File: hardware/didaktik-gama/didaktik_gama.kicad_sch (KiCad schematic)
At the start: 165 parts, among them J1 Klávesnice, J2 MG, J4 Porty 8255, J5 Napájení 9–12V DC, J7 VGA DE-15 (RGB 15 kHz), J8 RGB z modulu ULA, SW1 RESET, T1 KSY72, T2 KSY72, T3 KC507, U1 UA880D (Z80), U10 4164, U11 4164, U12 4164, U13 4164, U14 4164, U15 4164, U16 4164, U17 2118, U18 2118, U19 2118, U2 27128 (16K EPROM), U20 2118, U21 2118, U22 2118, U23 2118, U24 2118, U25 74LS04, U26 74LS04, U27 74LS00, U28 74LS10, U29 74LS32, U3 8255 (MHB8255), U32 R-78E5.0-1.0 (spínaný, náhrad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, U37 74HCT244, U38 74HCT08, U4 ULA, U5 74LS157, U6 74LS157, U7 74LS157, U8 74LS157, U9 4164, Y1 14MHz

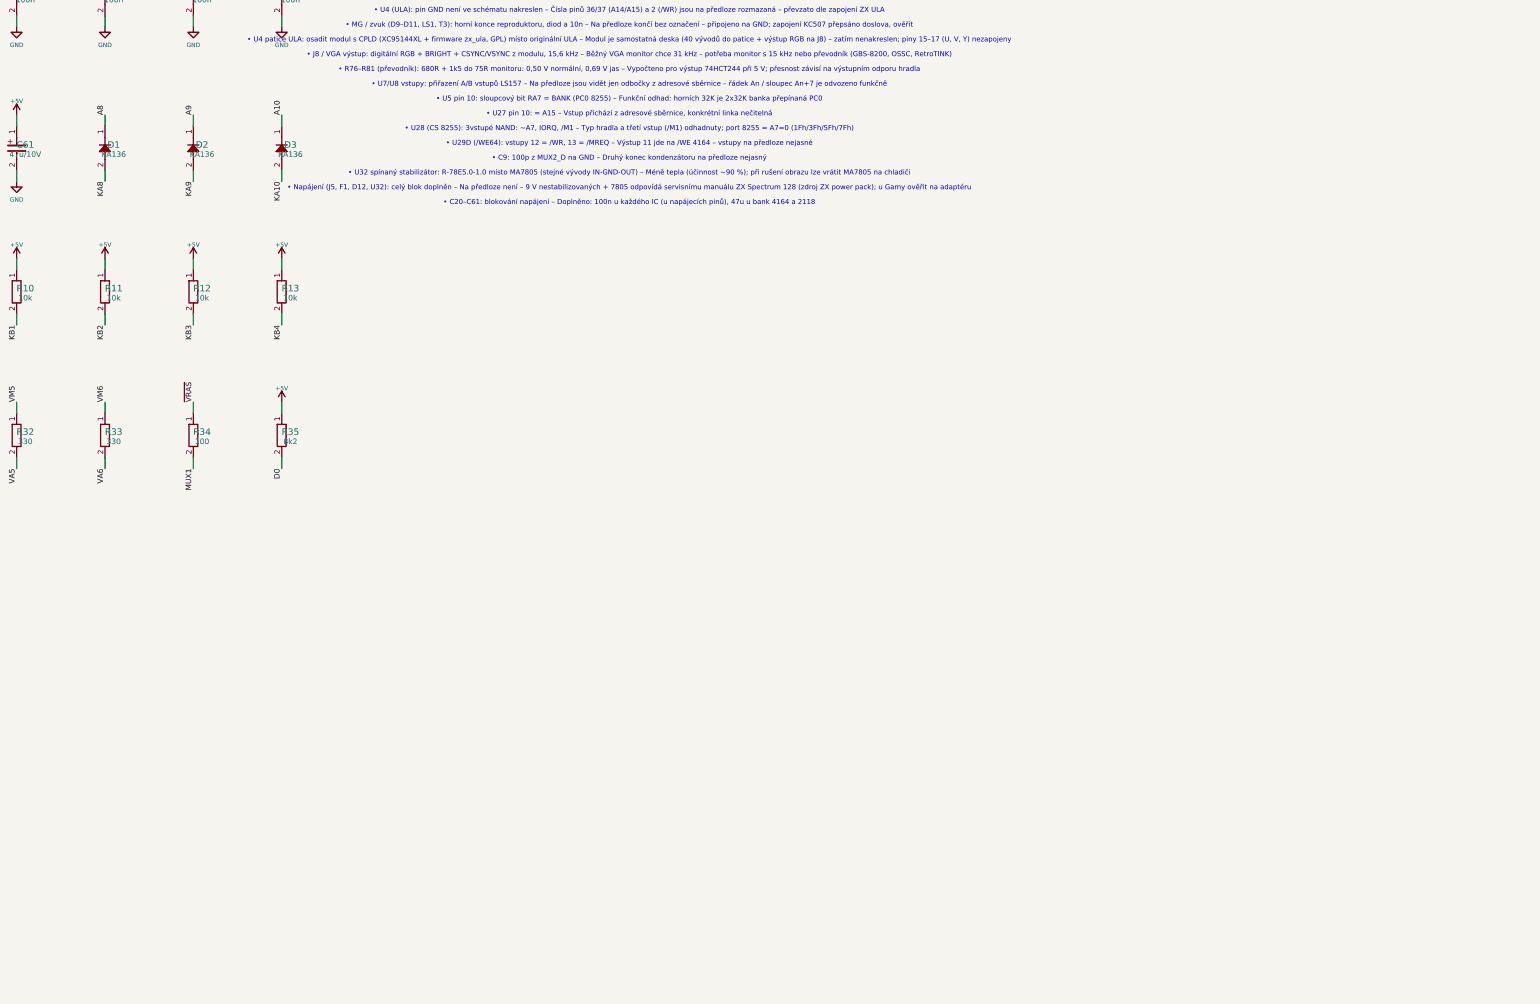
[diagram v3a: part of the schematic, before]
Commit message: Add USB keyboard interface (RPi Pico as USB host emulating the matrix)
Pico reads A8-A15 through 74LVC245 and pulls KB1-KB5 low through
open-drain 74LVC07, in parallel with the original keyboard; spare
buffer drives /RESET.

Co-Authored-By: Claude Opus 5.5 <noreply@anthropic.com>
Claude-Session: https://claude.ai/code/session_01LAVM7Gq9EYiUXiCEdy9ZRx
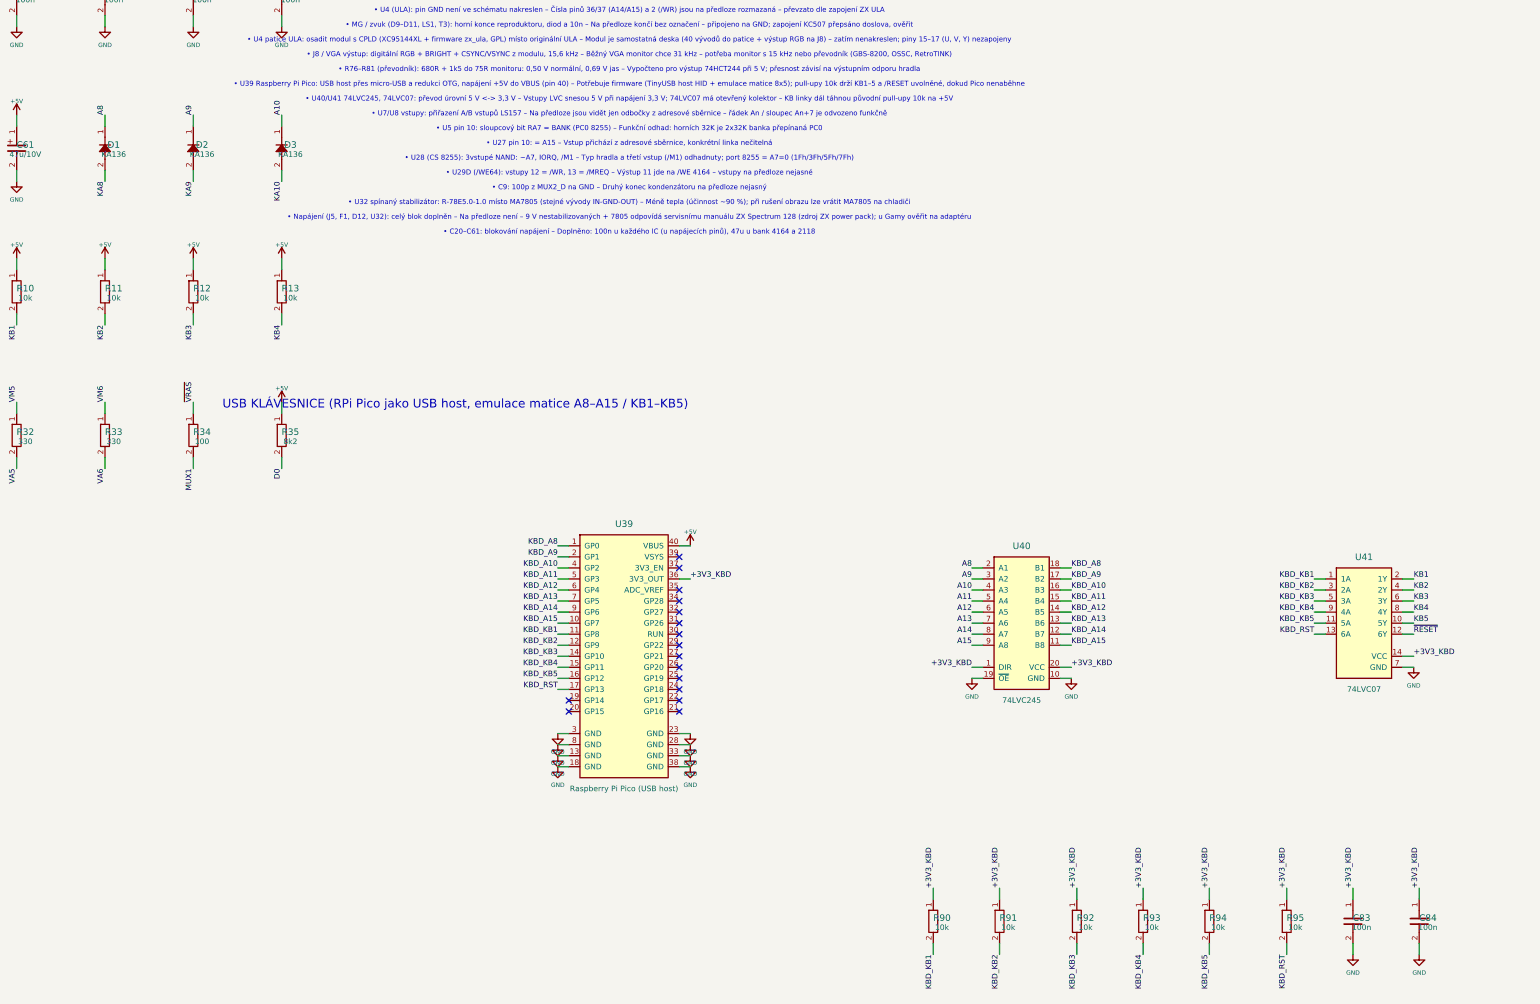
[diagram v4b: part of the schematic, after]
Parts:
- removed C12: 100n, Capacitor_THT:C_Disc_D5.0mm_W2.5mm_P5.00mm, symbol gama:C
- removed R19: 470, Resistor_THT:R_Axial_DIN0207_L6.3mm_D2.5mm_P10.16mm_Horizontal, symbol gama:R
- removed R33: 330, Resistor_THT:R_Axial_DIN0207_L6.3mm_D2.5mm_P10.16mm_Horizontal, symbol gama:R
- removed unit 2 of U25
- removed unit 4 of U28
- removed U32: R-78E5.0-1.0 (spínaný, náhrada 7805), Converter_DCDC:Converter_DCDC_RECOM_R-78E-0.5_THT, symbol gama:7805
- added C21, C44, C45, C83, C84: 100n, Capacitor_THT:C_Disc_D5.0mm_W2.5mm_P5.00mm, symbol gama:C
- added J5: Napájení 9–12V DC, Connector_BarrelJack:BarrelJack_Horizontal, symbol gama:CONN_2
- added R41: 8k2, Resistor_THT:R_Axial_DIN0207_L6.3mm_D2.5mm_P10.16mm_Horizontal, symbol gama:R
- added R90, R91, R92, R93, R94, R95: 10k, Resistor_THT:R_Axial_DIN0207_L6.3mm_D2.5mm_P10.16mm_Horizontal, symbol gama:R
- added U39: Raspberry Pi Pico (USB host), symbol gama:PICO
- added U40: 74LVC245, Package_SO:SOIC-20W_7.5x12.8mm_P1.27mm, symbol gama:74LVC245
- added U41: 74LVC07, Package_SO:SOIC-14_3.9x8.7mm_P1.27mm, symbol gama:74LVC07
- added U6: 74LS157, Package_DIP:DIP-16_W7.62mm, symbol gama:74LS157
- R19: renamed from U6; value 74LS157 -> 470; footprint Package_DIP:DIP-16_W7.62mm -> Resistor_THT:R_Axial_DIN0207_L6.3mm_D2.5mm_P10.16mm_Horizontal; symbol gama:74LS157 -> gama:R
- R33: renamed from U12; value 4164 -> 330; footprint Package_DIP:DIP-16_W7.62mm -> Resistor_THT:R_Axial_DIN0207_L6.3mm_D2.5mm_P10.16mm_Horizontal; symbol gama:4164 -> gama:R
- U12: renamed from R41; value 8k2 -> 4164; footprint Resistor_THT:R_Axial_DIN0207_L6.3mm_D2.5mm_P10.16mm_Horizontal -> Package_DIP:DIP-16_W7.62mm; symbol gama:R -> gama:4164
- U25: renamed from J5; value Napájení 9–12V DC -> 74LS04; footprint Connector_BarrelJack:BarrelJack_Horizontal -> Package_DIP:DIP-14_W7.62mm; symbol gama:CONN_2 -> gama:7404
- U28: renamed from C21; value 100n -> 74LS10; footprint Capacitor_THT:C_Disc_D5.0mm_W2.5mm_P5.00mm -> Package_DIP:DIP-14_W7.62mm; symbol gama:C -> gama:7410
- U32: renamed from C45; value 100n -> R-78E5.0-1.0 (spínaný, náhrada 7805); footprint Capacitor_THT:C_Disc_D5.0mm_W2.5mm_P5.00mm -> Converter_DCDC:Converter_DCDC_RECOM_R-78E-0.5_THT; symbol gama:C -> gama:7805
- renumbered C44 to C12
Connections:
- net +5V: now also U12.8 (VCC), U28.14 (VCC), U32.3 (OUT), C21.1, C44.1, C45.1, R41.1, U39.40 (VBUS), U6.16 (VCC); no longer C12.1, R19.16 (VCC), R33.8 (VCC), U12.1, U28.1, U32.1
- net A10: now also U40.4 (A3)
- net A11: now also U40.5 (A4), U6.10 (3B); no longer R19.10 (3B)
- net A12: now also U40.6 (A5), U6.6 (2B); no longer R19.6 (2B)
- net A13: now also U40.7 (A6), U6.3 (1B); no longer R19.3 (1B)
- net A14: now also U40.8 (A7), U6.13 (4B); no longer R19.13 (4B)
- net A15: now also U40.9 (A8)
- net A3: now also U6.11 (3A); no longer R19.11 (3A)
- net A4: now also U6.5 (2A); no longer R19.5 (2A)
- net A5: now also U6.2 (1A); no longer R19.2 (1A)
- net A6: now also U6.14 (4A); no longer R19.14 (4A)
- net A8: now also U40.2 (A1)
- net A9: now also U40.3 (A2)
- net D0: now also R19.1
- net D3: now also U12.14 (Q), U12.2 (D); no longer R33.14 (Q), R33.2 (D)
- net D6: now also R41.2; no longer U12.2
- net GND: now also U12.16 (GND), U28.7 (GND), C21.2, C44.2, C45.2, C83.2, C84.2, J5.2, U39.13 (GND), U39.18 (GND), U39.23 (GND), U39.28 (GND), U39.3 (GND), U39.33 (GND), U39.38 (GND), U39.8 (GND), U40.10 (GND), U40.19 (~{OE}), U41.7 (GND), U6.15 (~{G}), U6.8 (GND); no longer R19.15 (~{G}), R19.8 (GND), R33.16 (GND), U25.2, U28.2
- net KB1: now also U41.2 (1Y)
- net KB2: now also U41.4 (2Y)
- net KB3: now also U41.6 (3Y)
- net KB4: now also U41.8 (4Y)
- net KB5: now also U41.10 (5Y)
- net MUX2: now also U6.1 (S); no longer R19.1 (S)
- net RA0: now also U12.5 (A0); no longer R33.5 (A0)
- net RA1: now also U12.7 (A1); no longer R33.7 (A1)
- net RA2: now also U12.6 (A2); no longer R33.6 (A2)
- net RA3: now also U12.12 (A3), U6.9 (3Y); no longer R19.9 (3Y), R33.12 (A3)
- net RA4: now also U12.11 (A4), U6.7 (2Y); no longer R19.7 (2Y), R33.11 (A4)
- net RA5: now also U12.10 (A5), U6.4 (1Y); no longer R19.4 (1Y), R33.10 (A5)
- net RA6: now also U12.13 (A6), U6.12 (4Y); no longer R19.12 (4Y), R33.13 (A6)
- net RA7: now also U12.9 (A7); no longer R33.9 (A7)
- net VA6: now also R33.2
- net VD0: now also R19.2
- net VIN: now also C12.1, U32.1 (IN)
- net VIN_RAW: now also J5.1; no longer U25.1
- net VM6: now also R33.1
- net WR_D: now also U25.4
- net WR_I: now also U25.3
- net ~{CAS64}: now also U12.15 (~{CAS}); no longer R33.15 (~{CAS})
- net ~{RAS64}: now also U12.4 (~{RAS}); no longer R33.4 (~{RAS})
- net ~{RESET}: now also U41.12 (6Y)
- net ~{WE64}: now also U12.3 (~{WE}); no longer R33.3 (~{WE})
- new net +3V3_KBD: C83.1, C84.1, R90.1, R91.1, R92.1, R93.1, R94.1, R95.1, U39.36 (3V3_OUT), U40.1 (DIR), U40.20 (VCC), U41.14 (VCC)
- new net KBD_A10: U39.4 (GP2), U40.16 (B3)
- new net KBD_A11: U39.5 (GP3), U40.15 (B4)
- new net KBD_A12: U39.6 (GP4), U40.14 (B5)
- new net KBD_A13: U39.7 (GP5), U40.13 (B6)
- new net KBD_A14: U39.9 (GP6), U40.12 (B7)
- new net KBD_A15: U39.10 (GP7), U40.11 (B8)
- new net KBD_A8: U39.1 (GP0), U40.18 (B1)
- new net KBD_A9: U39.2 (GP1), U40.17 (B2)
- new net KBD_KB1: R90.2, U39.11 (GP8), U41.1 (1A)
- new net KBD_KB2: R91.2, U39.12 (GP9), U41.3 (2A)
- new net KBD_KB3: R92.2, U39.14 (GP10), U41.5 (3A)
- new net KBD_KB4: R93.2, U39.15 (GP11), U41.9 (4A)
- new net KBD_KB5: R94.2, U39.16 (GP12), U41.11 (5A)
- new net KBD_RST: R95.2, U39.17 (GP13), U41.13 (6A)
- no-connect marks 18 -> 34
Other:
- note added: "USB KLÁVESNICE (RPi Pico jako USB host, emulace matice A8–A15 / KB1–KB5)"
- note added: "• U39 Raspberry Pi Pico: USB host přes micro-USB a redukci OTG, napájení +5V do VBUS (pin 40) – Potřebuje firmware (TinyUSB host HID + emulace matice 8x5); pull-upy 10k drží KB1–5 a /RESET uvolněné, dokud Pico nenaběhne"
- note added: "• U40/U41 74LVC245, 74LVC07: převod úrovní 5 V <-> 3,3 V – Vstupy LVC snesou 5 V při napájení 3,3 V; 74LVC07 má otevřený kolektor – KB linky dál táhnou původní pull-upy 10k na +5V"
- moved on the sheet: C12, U25B
